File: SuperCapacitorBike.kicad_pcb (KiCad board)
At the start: 2 copper layers, 110.5 x 119.5 mm, 121 parts, among them J1 1988804, J10 1988862, J11 Barrel_Jack_Switch, J12 +5V, J13 1988862, J14 1988817, J2 GND, J3 RX, J4 TX, J5 RESET, J6 1988817, J7 1190363, J8 1190363, J9 1988862, K1 AWHSH105D00G, K2 AWHSH105D00G, Q1 IRFZ44N, Q2 IRFZ44N, Q3 IRFZ44N, Q4 IRFZ44N, Q5 IRFZ44N, Q6 IRFZ44N, Q7 GT065P06T, Q8 IRFZ44N, U1 IR2104, U10 L78L33_TO92, U2 IR2104, U3 IR2104, U4 UCC37324P, U5 MCP23017_SP, U6 ATmega328-P, U7 L7805, U8 ULN2003, U9 MCP4151-xxxx-P

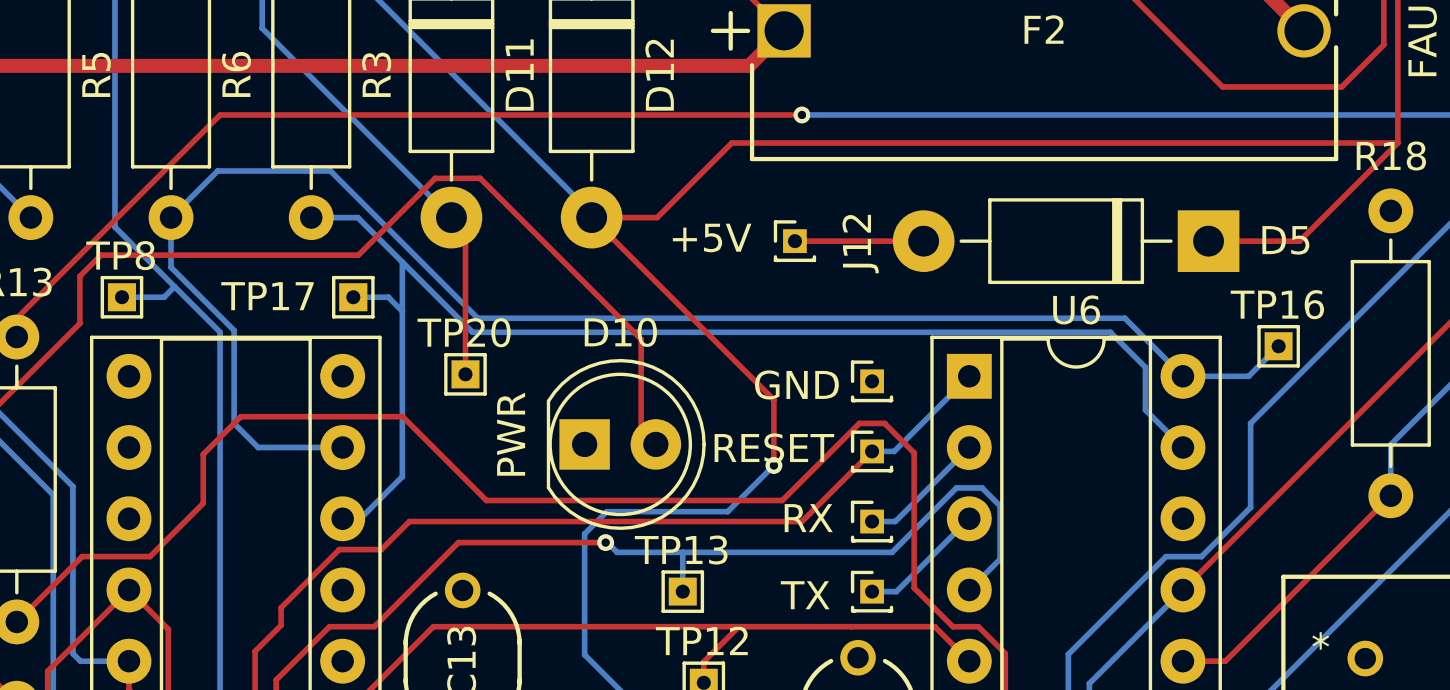
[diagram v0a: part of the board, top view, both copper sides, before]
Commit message: Fixed I2C error
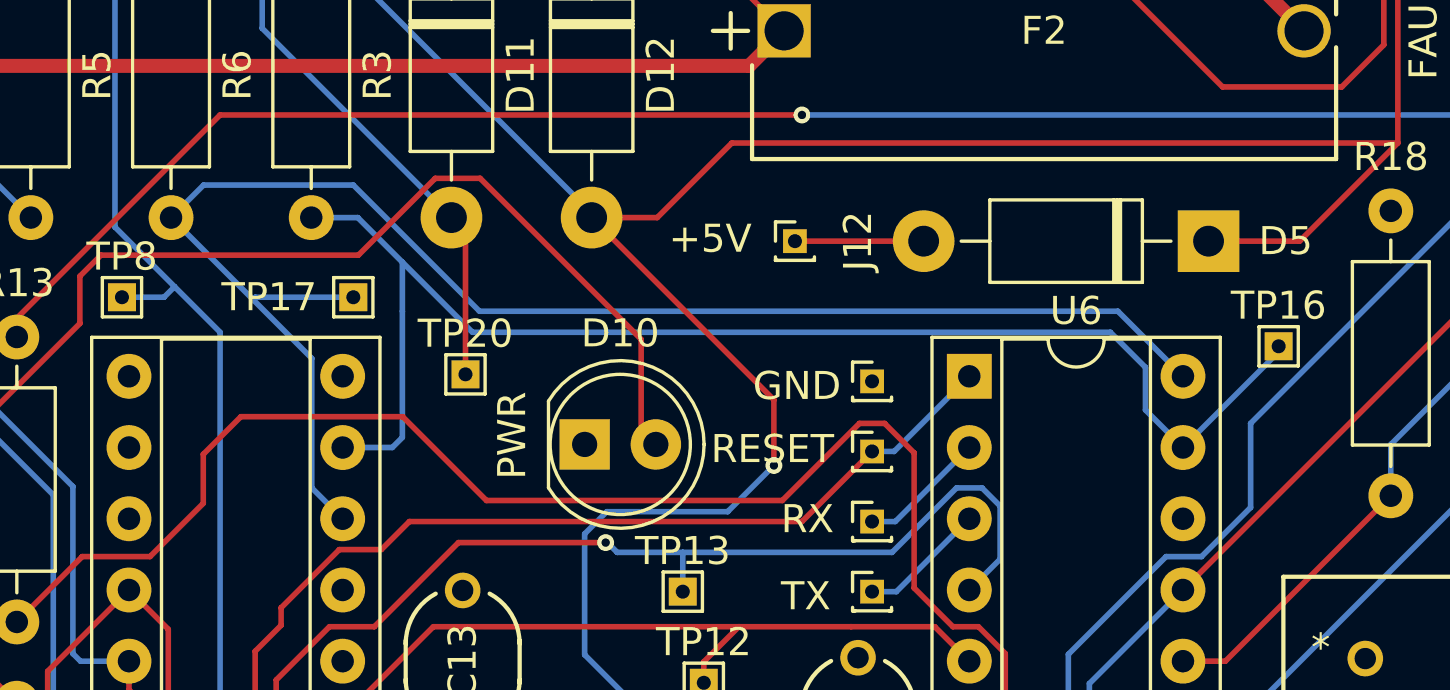
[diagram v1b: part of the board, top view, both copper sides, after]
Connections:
- TP16 pad 1: /Motor Controller/SCL -> /Motor Controller/SDA
- TP17 pad 1: /Motor Controller/SDA -> /Motor Controller/SCL
- U5 pad 12: /Motor Controller/SDA -> /Motor Controller/SCL
- U5 pad 13: /Motor Controller/SCL -> /Motor Controller/SDA
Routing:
- net /Motor Controller/SDA: track 47.1 -> 48.9 mm

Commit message: Reviewed gate resistors and removed MOSFET driver resistor
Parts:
- removed D11, D12: 1N5819, Diode_THT:D_DO-41_SOD81_P10.16mm_Horizontal
- removed R15: 47Ω, Resistor_THT:R_Axial_DIN0207_L6.3mm_D2.5mm_P10.16mm_Horizontal
- added D8: 1N5819, Diode_THT:D_DO-41_SOD81_P10.16mm_Horizontal, F.Cu at (81.0, 48.5)
- added D9: 1N5819, Diode_THT:D_DO-41_SOD81_P10.16mm_Horizontal, F.Cu at (76.0, 48.5)
- added TP14: TestPoint, TestPoint:TestPoint_THTPad_1.0x1.0mm_Drill0.5mm, F.Cu at (122.8, 84.7)
- moved R16 4.93 mm to (103.4, 101.5)
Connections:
- U4 pad 7: Net-(U4-OUTA) -> Net-(Q8-G)
- U6 pad 10: MOS_DRIVER -> unconnected-(U6-XTAL2/PB7-Pad10)
- U6 pad 18: unconnected-(U6-PB4-Pad18) -> MOS_DRIVER
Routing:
- net Net-(Q8-G): track 75.9 -> 98.1 mm
- net MOS_DRIVER: track 19.8 -> 33.0 mm, vias 0 -> 1
- net RELAY_1: track 92.6 -> 83.6 mm
- net Net-(U4-OUTA): track 7.55 -> 0.00 mm
- net +5V: track 512.1 -> 505.6 mm
- net ADC_C2V: track 67.8 -> 71.6 mm
- net +12V: track 244.3 -> 241.8 mm
- net RELAYS: track 47.8 -> 49.5 mm

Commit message: Prototyping PCB Ordered!
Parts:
- added R2: 0Ω, Resistor_THT:R_Axial_DIN0207_L6.3mm_D2.5mm_P10.16mm_Horizontal, F.Cu at (88.4, 104.3)
- added TP15: TestPoint, TestPoint:TestPoint_THTPad_1.0x1.0mm_Drill0.5mm, F.Cu at (125.8, 134.1)
- R10, R11, R12, R7, R8, R9: value 47Ω -> 10Ω
- moved TP31 36.5 mm to (107.3, 100.2)
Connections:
- TP31 pad 1: Net-(Q8-G) -> C1+
- U4 pad 7: Net-(Q8-G) -> Net-(U4-OUTA)
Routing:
- net Net-(Q8-G): track 98.1 -> 54.6 mm, vias 1 -> 0
- net Net-(U4-OUTA): track 0.00 -> 11.9 mm
- net C1+: track 126.9 -> 130.8 mm, vias 0 -> 1
- net SS1: track 179.0 -> 179.5 mm
